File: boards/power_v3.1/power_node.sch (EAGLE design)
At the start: 31 parts, among them J1 AVR_SPI_PRG_6NS, J2 12146734, U1 ATtiny167, U2 MCP2025, U3 MC17XSF500

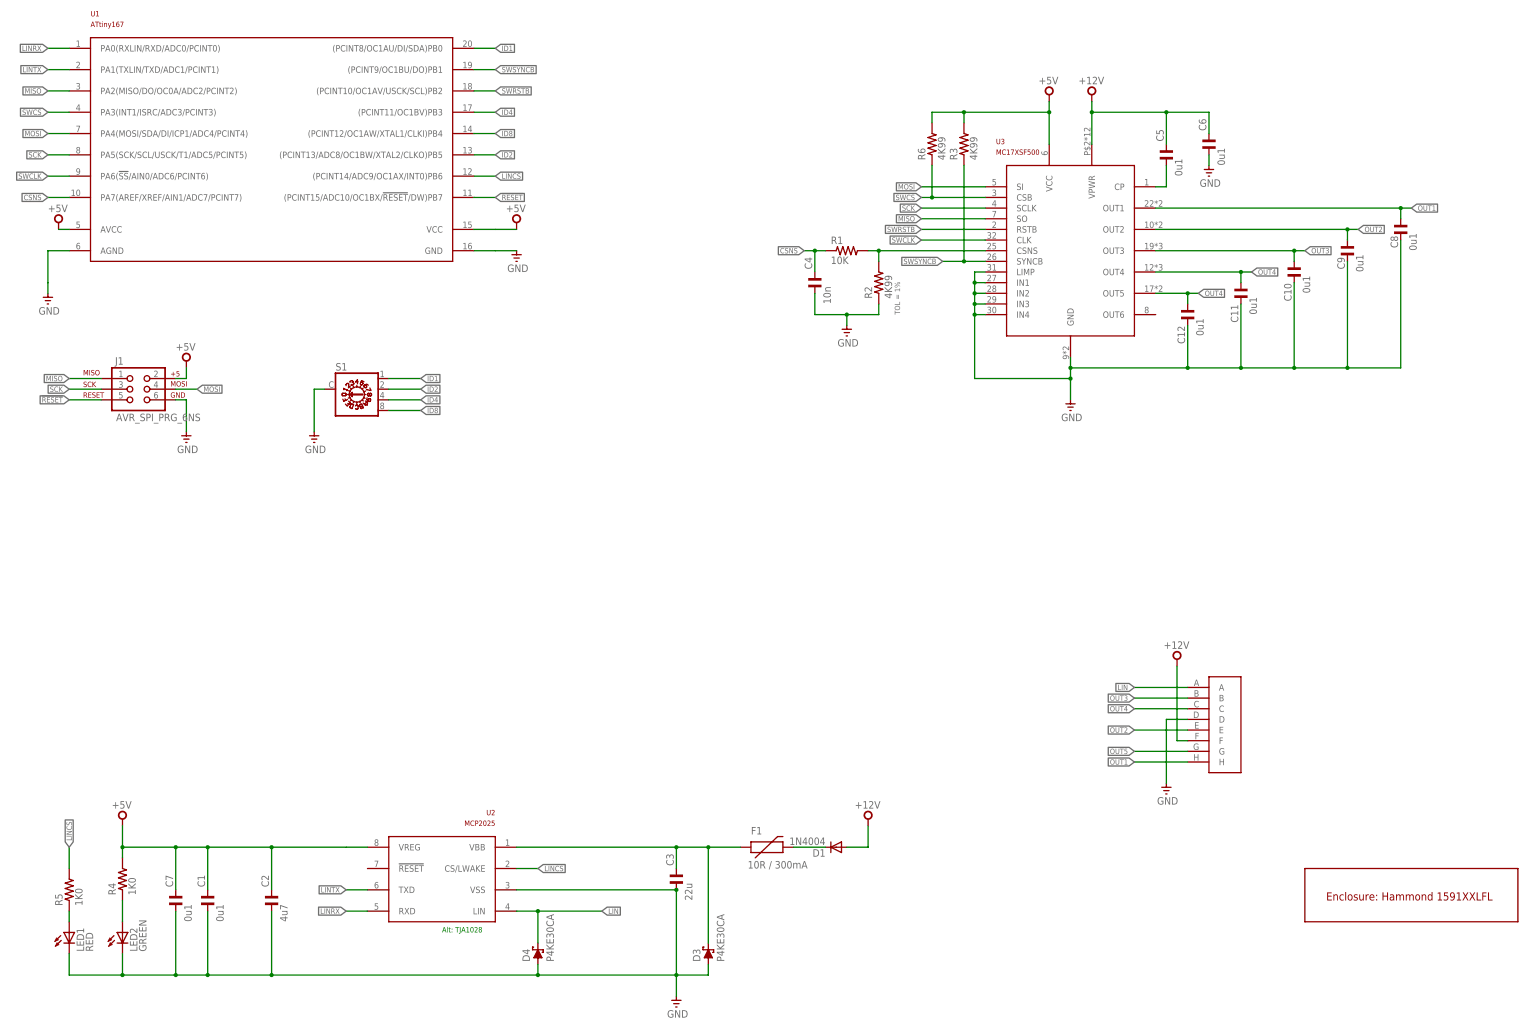
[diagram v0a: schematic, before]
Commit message: Spin the power_v3 board, add more support code for it
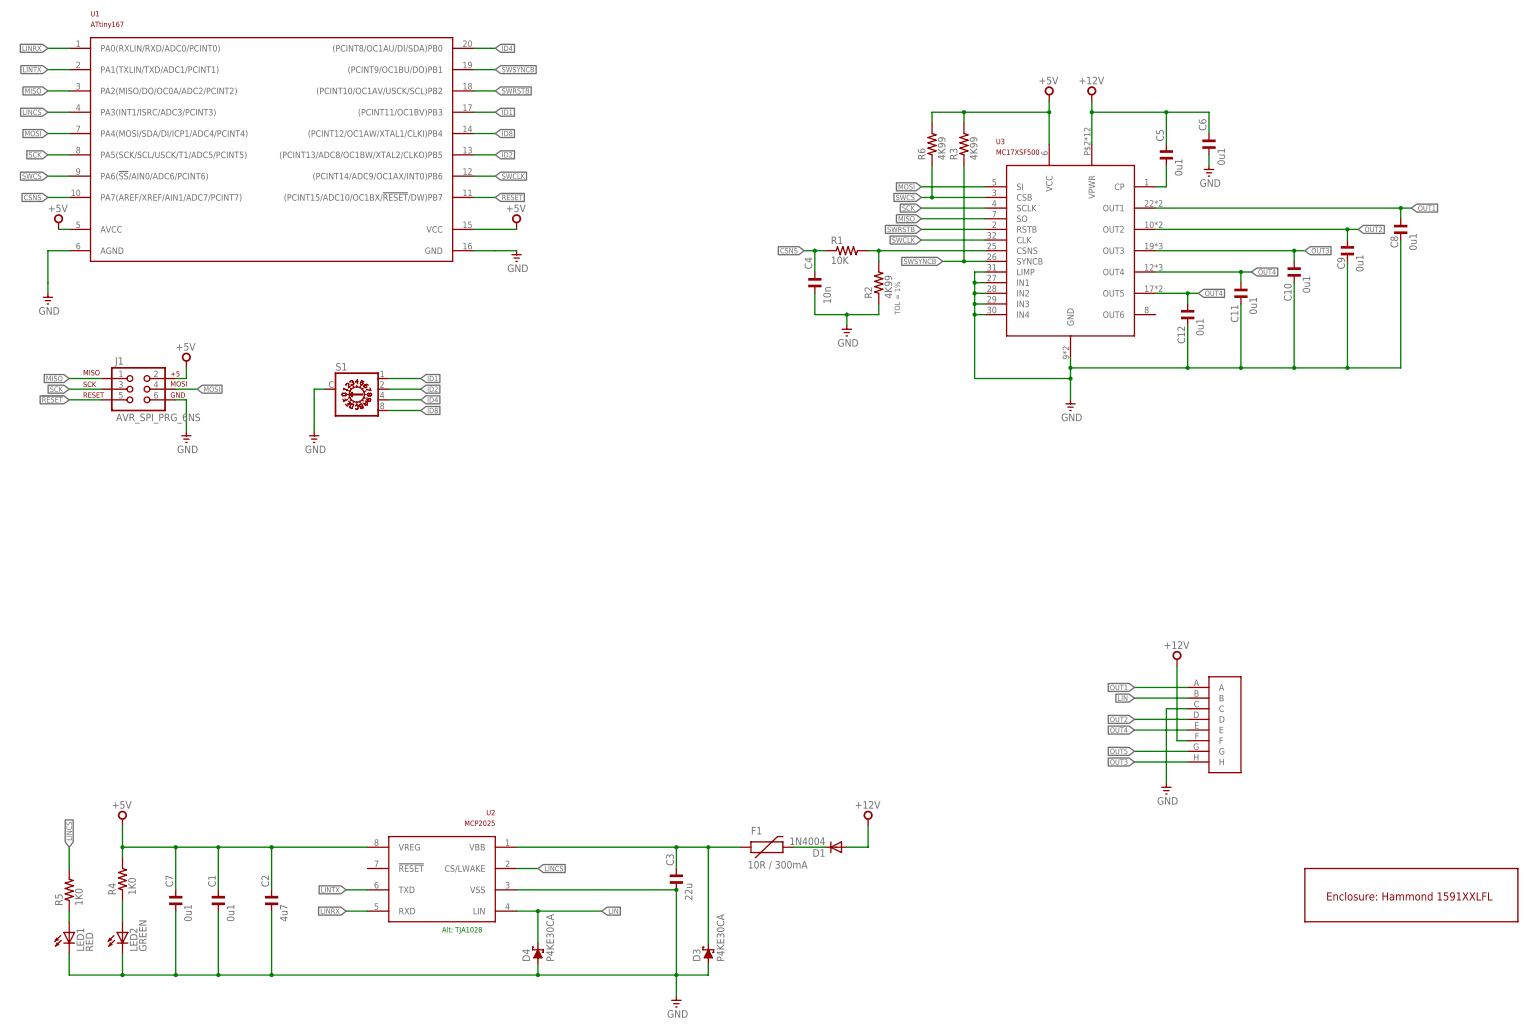
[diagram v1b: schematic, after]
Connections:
- net GND: now also J2.C; no longer J2.D
- net ID1: now also U1.(PCINT11/OC1BV)PB3; no longer U1.(PCINT8/OC1AU/DI/SDA)PB0
- net ID4: now also U1.(PCINT8/OC1AU/DI/SDA)PB0; no longer U1.(PCINT11/OC1BV)PB3
- net LIN: now also J2.B; no longer J2.A
- net LINCS: now also U1.PA3(INT1/ISRC/ADC3/PCINT3); no longer U1.(PCINT14/ADC9/OC1AX/INT0)PB6
- net OUT1: now also J2.A; no longer J2.H
- net OUT2: now also J2.D; no longer J2.E
- net OUT3: now also J2.H; no longer J2.B
- net OUT4: now also J2.E; no longer J2.C
- net SWCLK: now also U1.(PCINT14/ADC9/OC1AX/INT0)PB6; no longer U1.PA6(!SS!/AIN0/ADC6/PCINT6)
- net SWCS: now also U1.PA6(!SS!/AIN0/ADC6/PCINT6); no longer U1.PA3(INT1/ISRC/ADC3/PCINT3)
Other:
- moved on the sheet: C1
